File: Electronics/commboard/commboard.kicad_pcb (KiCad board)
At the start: 2 copper layers, 107.3 x 72.3 mm, 75 parts, among them J101 LED CONN, J102 ProximitySensorConnector, J103 STLINK, J104 RS232_Out, J107 Measurement Conn, J201 ServoConn, J301 ServoConn, J401 ServoConn, J501 InputConn, J601 USB_B, Q101 BC847, Q102 BSS83P, SW101 SW_Push, U101 STM32F070CBTx, U102 M24C08, U103 MAX3221, U201 SP3485EN, U301 SP3485EN, U401 SP3485EN, U501 LM2576HVS-3.3, Y101 8MHz

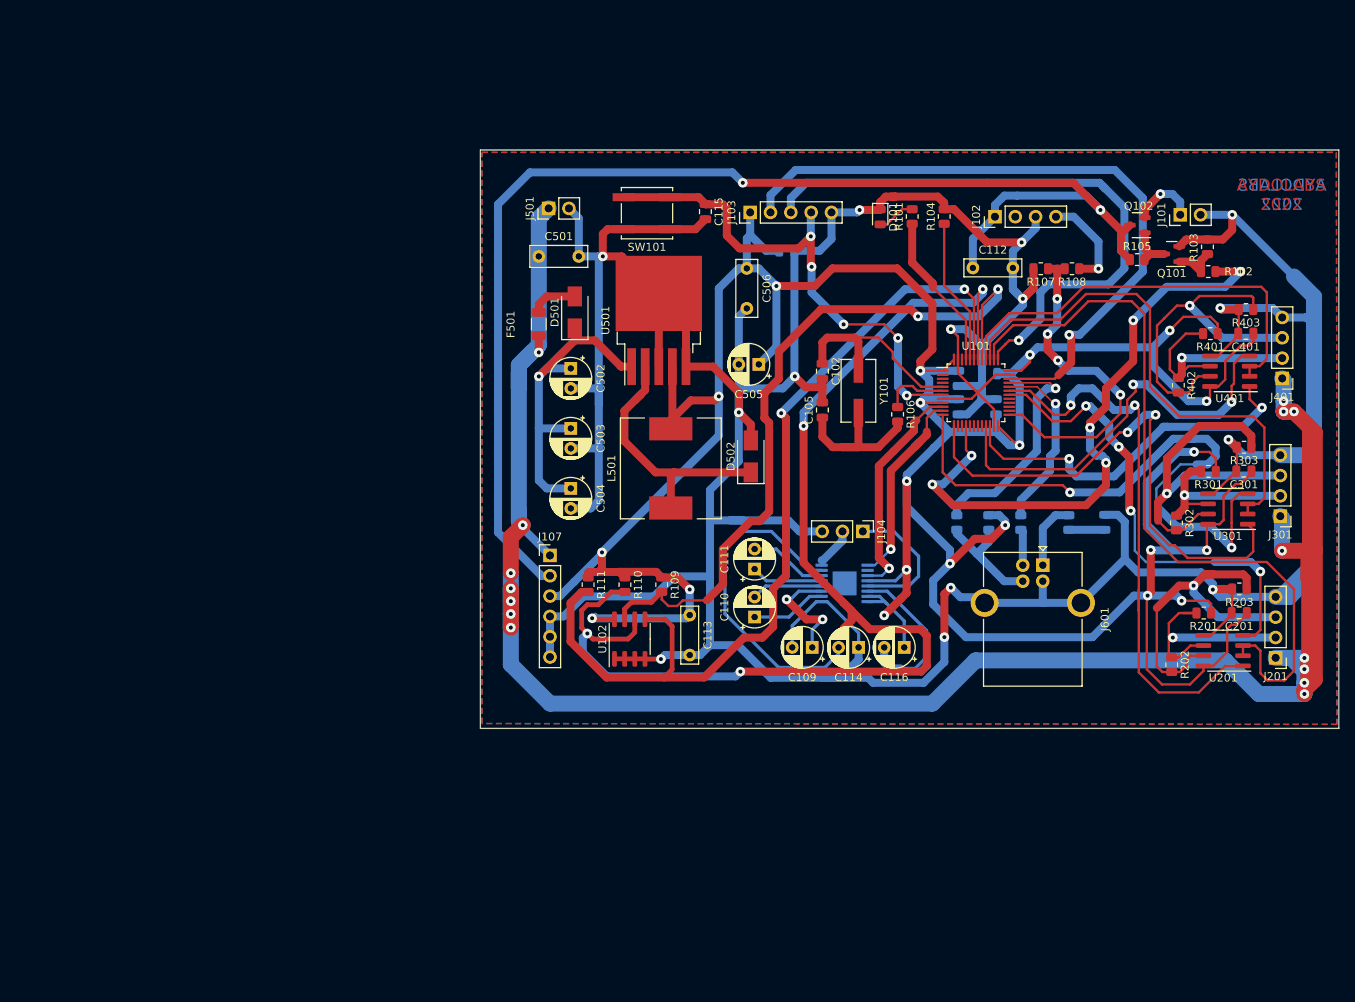
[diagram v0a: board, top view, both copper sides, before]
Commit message: schematic design completed. pcb layout drawings completed.
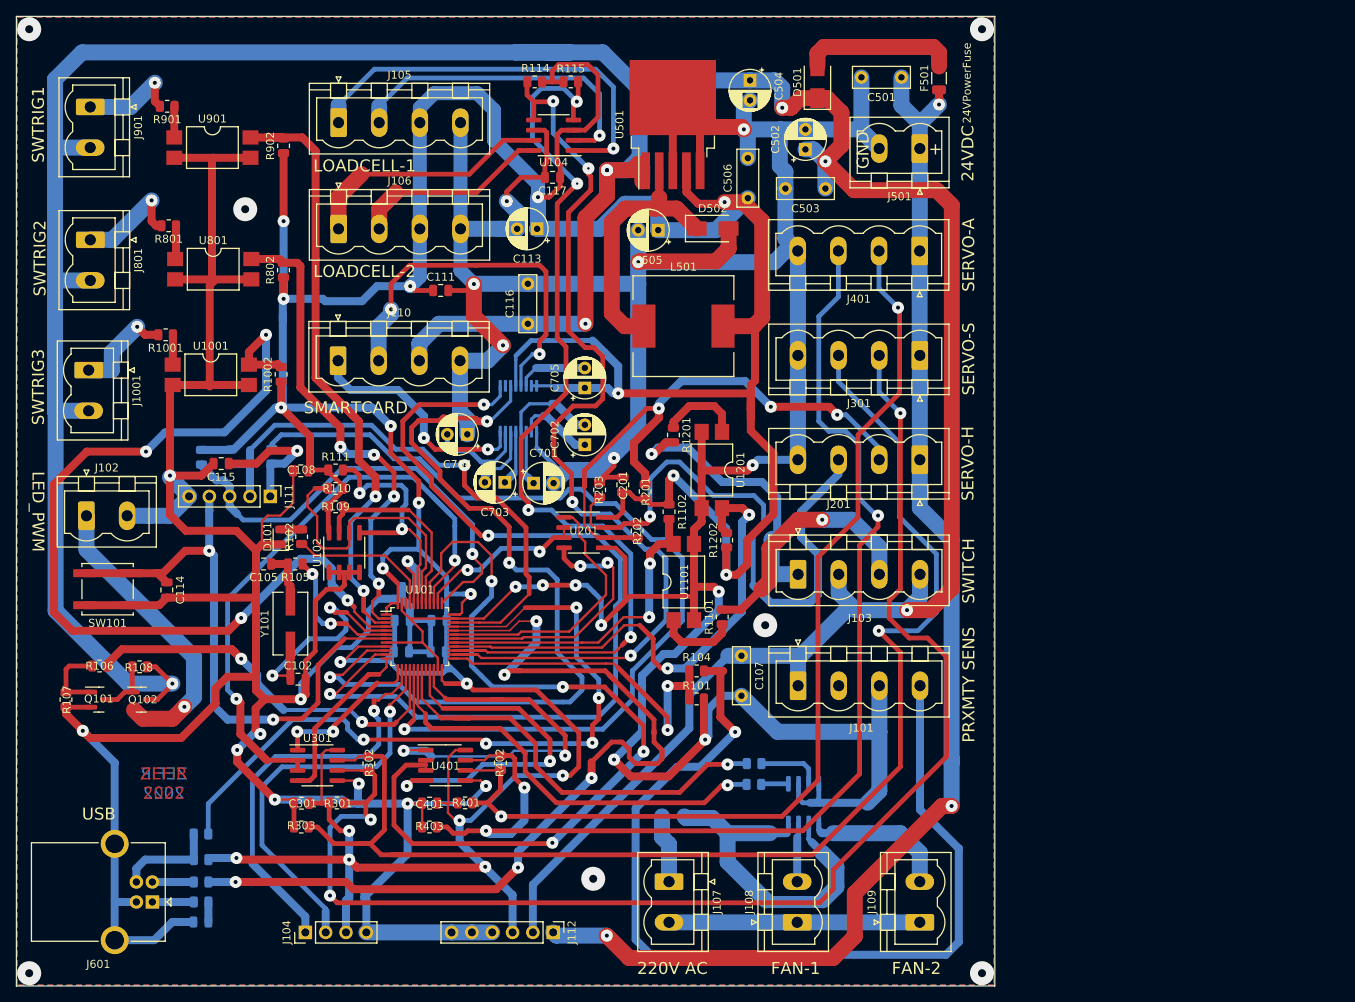
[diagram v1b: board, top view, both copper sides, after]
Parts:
- removed C110: 0.1uF, Capacitor_THT:CP_Radial_D5.0mm_P2.50mm
- removed C112: 100nF, Capacitor_THT:C_Rect_L7.0mm_W2.0mm_P5.00mm
- added C107: 100nF, Capacitor_THT:C_Rect_L7.0mm_W2.0mm_P5.00mm, F.Cu at (130.6, 119.9)
- added C117: 100nF, Capacitor_SMD:C_0805_2012Metric, F.Cu at (107.0, 60.1)
- added C701: 0.1uF, Capacitor_THT:CP_Radial_D5.0mm_P2.50mm, F.Cu at (104.6, 98.3)
- added C702: 0.1uF, Capacitor_THT:CP_Radial_D5.0mm_P2.50mm, F.Cu at (111.1, 93.5)
- added C703: 0.1uF, Capacitor_THT:CP_Radial_D5.0mm_P2.50mm, F.Cu at (101.1, 98.2)
- added C704: 0.1uF, Capacitor_THT:CP_Radial_D5.0mm_P2.50mm, F.Cu at (96.4, 92.2)
- added C705: 0.1uF, Capacitor_THT:CP_Radial_D5.0mm_P2.50mm, F.Cu at (111.1, 86.4)
- added F101: Fuse, Fuse:Fuse_1206_3216Metric, B.Cu at (122.1, 140.0)
- added J1001: EXTINT_PORT_0, Connector_Phoenix_MSTB:PhoenixContact_MSTBVA_2,5_2-G-5,08_1x02_P5.08mm_Vertical, F.Cu at (49.0, 84.2)
- added J105: LC_Conn_1, Connector_Phoenix_MSTB:PhoenixContact_MSTBVA_2,5_4-G-5,08_1x04_P5.08mm_Vertical, F.Cu at (80.3, 53.3)
- added J106: LC_Conn_2, Connector_Phoenix_MSTB:PhoenixContact_MSTBVA_2,5_4-G-5,08_1x04_P5.08mm_Vertical, F.Cu at (80.3, 66.6)
- added J108: FAN1, Connector_Phoenix_MSTB:PhoenixContact_MSTBVA_2,5_2-G-5,08_1x02_P5.08mm_Vertical, F.Cu at (137.6, 153.2)
- added J109: FAN2, Connector_Phoenix_MSTB:PhoenixContact_MSTBVA_2,5_2-G-5,08_1x02_P5.08mm_Vertical, F.Cu at (152.9, 153.2)
- added J110: RS232_Out, Connector_Phoenix_MSTB:PhoenixContact_MSTBVA_2,5_4-G-5,08_1x04_P5.08mm_Vertical, F.Cu at (80.2, 83.0)
- added J111: STLINK, Connector_PinHeader_2.54mm:PinHeader_1x05_P2.54mm_Vertical, F.Cu at (71.7, 100.0)
- added J112: Measurement Conn, Connector_PinHeader_2.54mm:PinHeader_1x06_P2.54mm_Vertical, F.Cu at (107.1, 154.5)
- added J801: EXTINT_PORT_0, Connector_Phoenix_MSTB:PhoenixContact_MSTBVA_2,5_2-G-5,08_1x02_P5.08mm_Vertical, F.Cu at (49.2, 67.9)
- added J901: EXTINT_PORT_0, Connector_Phoenix_MSTB:PhoenixContact_MSTBVA_2,5_2-G-5,08_1x02_P5.08mm_Vertical, F.Cu at (49.2, 51.3)
- added R1001: 1kR, Resistor_SMD:R_0805_2012Metric, F.Cu at (58.7, 79.8)
- added R1002: 4k7R, Resistor_SMD:R_0805_2012Metric, F.Cu at (73.1, 84.7)
- added R1101: 470R, Resistor_SMD:R_0805_2012Metric, F.Cu at (128.2, 115.1)
- added R1102: 4k7R, Resistor_SMD:R_0805_2012Metric, F.Cu at (121.6, 101.9)
- added R112: 120R, Resistor_SMD:R_0805_2012Metric, B.Cu at (132.2, 136.0)
- added R113: 120R, Resistor_SMD:R_0805_2012Metric, B.Cu at (132.2, 133.4)
- added R114: 4k7, Resistor_SMD:R_0805_2012Metric, F.Cu at (104.8, 48.2)
- added R115: 4k7, Resistor_SMD:R_0805_2012Metric, F.Cu at (109.3, 48.2)
- added R116: 4k7, Resistor_SMD:R_0805_2012Metric, B.Cu at (63.1, 95.1)
- added R117: 4k7, Resistor_SMD:R_0805_2012Metric, B.Cu at (66.8, 95.0)
- added R118: 470R, Resistor_SMD:R_0805_2012Metric, B.Cu at (71.9, 95.0)
- added R1201: 470R, Resistor_SMD:R_0805_2012Metric, F.Cu at (122.1, 92.3)
- added R1202: 4k7R, Resistor_SMD:R_0805_2012Metric, F.Cu at (128.8, 105.5)
- added R801: 1kR, Resistor_SMD:R_0805_2012Metric, F.Cu at (59.0, 66.2)
- added R802: 4k7R, Resistor_SMD:R_0805_2012Metric, F.Cu at (73.4, 71.7)
- added R901: 1kR, Resistor_SMD:R_0805_2012Metric, F.Cu at (58.9, 51.2)
- added R902: 4k7R, Resistor_SMD:R_0805_2012Metric, F.Cu at (73.4, 56.2)
- added U1001: LTV-817S, Package_DIP:SMDIP-4_W9.53mm, F.Cu at (64.3, 84.8)
- added U104: MCP3426-xMC, Package_SO:SOIC-8_3.9x4.9mm_P1.27mm, F.Cu at (107.2, 54.9)
- added U1101: LTV-817S, Package_DIP:SMDIP-4_W9.53mm, F.Cu at (123.4, 110.7)
- added U1201: LTV-817S, Package_DIP:SMDIP-4_W9.53mm, F.Cu at (126.9, 96.7)
- added U701: MAX3221, Package_SO:TSSOP-16_4.4x5mm_P0.65mm, B.Cu at (102.8, 89.0)
- added U801: LTV-817S, Package_DIP:SMDIP-4_W9.53mm, F.Cu at (64.6, 71.6)
- added U901: LTV-817S, Package_DIP:SMDIP-4_W9.53mm, F.Cu at (64.5, 56.4)
- C108: moved to F.Cu
- C109: value 0.1uF -> 100nF; footprint Capacitor_THT:CP_Radial_D5.0mm_P2.50mm -> Capacitor_SMD:C_0805_2012Metric; moved to B.Cu
- C111, C114: value 0.1uF -> 100nF; footprint Capacitor_THT:CP_Radial_D5.0mm_P2.50mm -> Capacitor_SMD:C_0805_2012Metric
- C113: value 100nF -> 100uF; footprint Capacitor_THT:C_Rect_L7.0mm_W2.0mm_P5.00mm -> Capacitor_THT:CP_Radial_D5.0mm_P2.50mm
- C116: value 0.1uF -> 100nF; footprint Capacitor_THT:CP_Radial_D5.0mm_P2.50mm -> Capacitor_THT:C_Rect_L7.0mm_W2.0mm_P5.00mm
- C503: footprint Capacitor_THT:CP_Radial_D5.0mm_P2.50mm -> Capacitor_THT:C_Rect_L7.0mm_W2.5mm_P5.00mm
- J101: value LED CONN -> ProximitySensorConnector; footprint Connector_PinHeader_2.54mm:PinHeader_1x02_P2.54mm_Vertical -> Connector_Phoenix_MSTB:PhoenixContact_MSTBVA_2,5_4-G-5,08_1x04_P5.08mm_Vertical
- J102: value ProximitySensorConnector -> PWM CONN; footprint Connector_PinHeader_2.54mm:PinHeader_1x04_P2.54mm_Vertical -> Connector_Phoenix_MSTB:PhoenixContact_MSTBVA_2,5_2-G-5,08_1x02_P5.08mm_Vertical
- J103: value STLINK -> InputArray; footprint Connector_PinHeader_2.54mm:PinHeader_1x05_P2.54mm_Vertical -> Connector_Phoenix_MSTB:PhoenixContact_MSTBVA_2,5_4-G-5,08_1x04_P5.08mm_Vertical
- J104: value RS232_Out -> ADC_Interface; footprint Connector_PinHeader_2.54mm:PinHeader_1x03_P2.54mm_Vertical -> Connector_PinHeader_2.54mm:PinHeader_1x04_P2.54mm_Vertical
- J107: value Measurement Conn -> AC 220V; footprint Connector_PinHeader_2.54mm:PinHeader_1x06_P2.54mm_Vertical -> Connector_Phoenix_MSTB:PhoenixContact_MSTBVA_2,5_2-G-5,08_1x02_P5.08mm_Vertical
- J201, J301, J401: footprint Connector_PinHeader_2.54mm:PinHeader_1x04_P2.54mm_Vertical -> Connector_Phoenix_MSTB:PhoenixContact_MSTBVA_2,5_4-G-5,08_1x04_P5.08mm_Vertical
- J501: footprint Connector_PinHeader_2.54mm:PinHeader_1x02_P2.54mm_Vertical -> Connector_Phoenix_MSTB:PhoenixContact_MSTBVA_2,5_2-G-5,08_1x02_P5.08mm_Vertical
- R101: value 2k2R -> 4k7R
- R102: value 470R -> 2k2R
- R103: moved to B.Cu
- R104: value 10k -> 620R
- R105: value 4k7R -> 390R
- R106: value 390R -> 470R
- R107: value 4k7R -> 10k
- R108: value 620R -> 4k7R
- U103: value MAX3221 -> CPC1961GS; footprint Package_SO:HTSSOP-16-1EP_4.4x5mm_P0.65mm_EP3x3mm -> Package_SO:SOIC-8_3.9x4.9mm_P1.27mm
- moved Q101 145.2 mm to (50.3, 125.4), turned to 0 degrees
- moved Q102 137.9 mm to (55.6, 125.4), turned to 0 degrees
- moved R107 133.2 mm to (46.2, 125.4), turned to -90 degrees
- moved R303 127.1 mm to (75.6, 141.3)
- moved R108 126.7 mm to (55.4, 121.3)
- moved C301 124.9 mm to (75.6, 138.3)
- moved D601 123.5 mm to (63.1, 153.2), turned to 0 degrees
- moved R403 120.8 mm to (91.6, 141.3)
- moved J102 119.6 mm to (48.8, 102.4), turned to 0 degrees
- moved J601 119.0 mm to (57.0, 150.7), turned to 180 degrees
- moved R601 118.4 mm to (63.1, 150.7), turned to 0 degrees
- moved U301 118.2 mm to (77.6, 133.6), turned to 0 degrees
- moved R102 118.1 mm to (75.7, 105.0), turned to 90 degrees
- moved C401 117.7 mm to (91.7, 138.3)
- moved R301 116.6 mm to (80.1, 138.3), turned to 0 degrees
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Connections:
- net I2C_SCL renamed EEPROM_SCL
- net I2C_SDA renamed EEPROM_SDA
- C109 pad 1: Net-(C109-Pad1) -> +3.3V
- C111 pad 1: Net-(C111-Pad1) -> +3.3V
- C111 pad 2: Net-(C111-Pad2) -> GND
- C114 pad 1: GND -> NRST
- C114 pad 2: Net-(C114-Pad2) -> GND
- C115 pad 1: NRST -> Net-(J111-Pad1)
- C116 pad 1: +3.3V -> 24V_Safe
- C116 pad 2: Net-(C116-Pad2) -> GND
- C502 pad 1: Net-(C502-Pad1) -> 24V_Safe
- C503 pad 1: Net-(C502-Pad1) -> 24V_Safe
- C504 pad 1: Net-(C502-Pad1) -> 24V_Safe
- D501 pad 1: Net-(C502-Pad1) -> 24V_Safe
- J101 pad 1: Net-(J101-Pad1) -> 24V_Safe
- J101 pad 2: GND -> unconnected-(J101-Pad2)
- J102 pad 1: 24V_Safe -> Net-(J102-Pad1)
- J102 pad 2: unconnected-(J102-Pad2) -> GND
- J103 pad 1: +3.3V -> /InputModuleNC3/SW
- J103 pad 2: SWDIO -> 24V_Safe
- J103 pad 3: SWCLK -> /InputModuleNC/SW
- J103 pad 4: NRST -> 24V_Safe
- J104 pad 1: Net-(J104-Pad1) -> ADC0
- J104 pad 2: Net-(J104-Pad2) -> ADC1
- J104 pad 3: GND -> +3.3V
- J107 pad 1: 24V_Unsafe -> Net-(J107-Pad1)
- J107 pad 2: 24V_Safe -> Net-(J107-Pad2)
- Q102 pad 2: Net-(J101-Pad1) -> Net-(J102-Pad1)
- R101 pad 1: Net-(R101-Pad1) -> objectSensorPin
- R101 pad 2: Net-(D101-Pad2) -> GND
- R102 pad 1: LedPWMPin -> Net-(R102-Pad1)
- R102 pad 2: Net-(Q101-Pad1) -> Net-(D101-Pad2)
- R103 pad 1: Net-(Q101-Pad1) -> Net-(R103-Pad1)
- R104 pad 1: Net-(R104-Pad1) -> Net-(J101-Pad4)
- R104 pad 2: GND -> objectSensorPin
- R105 pad 1: 24V_Safe -> Net-(R105-Pad1)
- R105 pad 2: Net-(Q101-Pad3) -> Net-(C105-Pad1)
- R106 pad 1: Net-(R106-Pad1) -> LedPWMPin
- R106 pad 2: Net-(C105-Pad1) -> Net-(Q101-Pad1)
- R107 pad 1: objectSensorPin -> Net-(Q101-Pad1)
- R108 pad 1: Net-(J102-Pad4) -> 24V_Safe
- R108 pad 2: objectSensorPin -> Net-(Q101-Pad3)
- U101 pad 14: Out0 -> ADC0
- U101 pad 15: Out1 -> ADC1
- U101 pad 17: PWM2 -> DebuggerSens
- U101 pad 18: PWM3 -> AC_DRV1
- U101 pad 19: PWM4 -> AC_DRV2
- U101 pad 2: unconnected-(U101-Pad2) -> EXTINT0
- U101 pad 20: Out2 -> unconnected-(U101-Pad20)
- U101 pad 26: In0 -> LOADCELL_SCL
- U101 pad 27: In1 -> LOADCELL_SDA
- U101 pad 28: In2 -> SW_In0
- U101 pad 29: In3 -> SW_In1
- U101 pad 3: unconnected-(U101-Pad3) -> EXTINT1
- U101 pad 4: unconnected-(U101-Pad4) -> EXTINT2
- U101 pad 44: Net-(R104-Pad1) -> Net-(R103-Pad1)
- U101 pad 45: Net-(R101-Pad1) -> Net-(R102-Pad1)
- U101 pad 6: Net-(R106-Pad1) -> Net-(R105-Pad1)
- U103 pad 1: GND -> Net-(R112-Pad1)
- U103 pad 2: Net-(C110-Pad1) -> GND
- U103 pad 3: Net-(C109-Pad1) -> Net-(R113-Pad1)
- U103 pad 4: Net-(C110-Pad2) -> GND
- U103 pad 5: Net-(C111-Pad1) -> Net-(J109-Pad2)
- U103 pad 6: Net-(C111-Pad2) -> Net-(U103-Pad6)
- U103 pad 7: Net-(C114-Pad2) -> Net-(J108-Pad2)
- U103 pad 8: Net-(J104-Pad2) -> Net-(U103-Pad6)
- U501 pad 1: Net-(C502-Pad1) -> 24V_Safe
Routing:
- net 24V_Safe: track 161.3 -> 461.1 mm, vias 2 -> 7
- net GND: track 651.7 -> 912.9 mm, vias 14 -> 23
- net +3.3V: track 473.9 -> 623.6 mm
- net 24V_Unsafe: track 310.1 -> 161.7 mm, vias 15 -> 3
- net Net-(J301-Pad2): track 24.2 -> 171.9 mm, vias 1 -> 3
- net LOADCELL_SDA: track 0.00 -> 122.7 mm, vias 0 -> 4
- net LOADCELL_SCL: track 0.00 -> 122.6 mm, vias 0 -> 4
- net Net-(J101-Pad4): track 0.00 -> 119.6 mm, vias 0 -> 1
- net DebuggerSens: track 0.00 -> 117.9 mm, vias 0 -> 1
- net EXTINT2: track 0.00 -> 114.2 mm, vias 0 -> 4
- net EEPROM_SCL: track 149.1 -> 36.1 mm, vias 4 -> 0
- net Net-(J301-Pad3): track 54.5 -> 163.6 mm
- net Net-(J401-Pad3): track 43.8 -> 148.9 mm, vias 1 -> 3
- net USBD-: track 22.4 -> 122.4 mm, vias 1 -> 5
- net Net-(J401-Pad2): track 28.9 -> 126.4 mm, vias 1 -> 2
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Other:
- board size 107.3 x 72.3 mm -> 122.3 x 121.2 mm
- board text added: "+"
- board text added: "220V AC"
- board text added: "24VDC"
- board text added: "FAN-1"
- board text added: "FAN-2"
- board text added: "GND"
- board text added: "LED_PWM"
- board text added: "LOADCELL-1"
- board text added: "LOADCELL-2"
- board text added: "PRXMTY SENS"
- board text added: "SERVO-A"
- board text added: "SERVO-H"
- board text added: "SERVO-S"
- board text added: "SMARTCARD"
- board text added: "SWITCH"
- board text added: "SWTRIG1"
- board text added: "SWTRIG2"
- board text added: "SWTRIG3"
- board text added: "USB"
- board text added: "ZEFIR 2022"
- board text removed: "AYDOLABS 2022"
